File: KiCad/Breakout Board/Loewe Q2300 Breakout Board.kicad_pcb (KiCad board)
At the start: 2 copper layers, 61 x 12.7 mm, 2 parts, among them J1 VGA DSUB-15, J2 JST_XH_1x10_P2.54mm_Horizontal

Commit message: Add version to PCB silkscreen.
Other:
- board text added: "Loewe Q2300 Breakout Board V.1.0"
- board text removed: "Loewe Q2300 Breakout Board"
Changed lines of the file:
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@@
 		(layer "Edge.Cuts")
 	)
-	(gr_text "Loewe Q2300\nBreakout Board"
+	(gr_text "Loewe Q2300\nBreakout Board V.1.0"
 		(at 160.35 95.95 0)
 		(layer "B.SilkS")

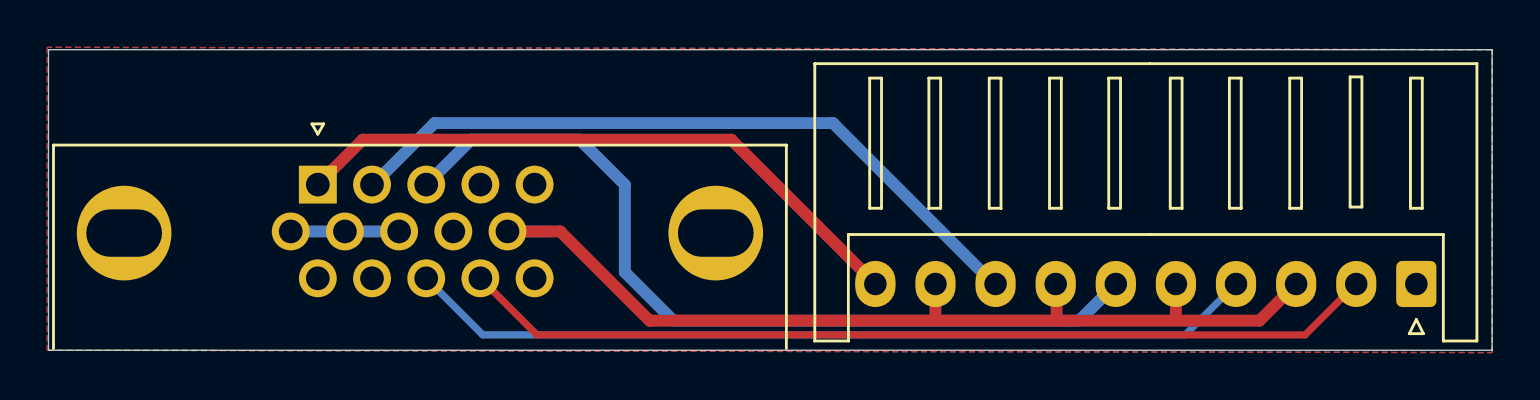
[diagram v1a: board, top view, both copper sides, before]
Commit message: Replace incorrect Connector_Dsub:DSUB-15-HD_Male with Connector_Dsub:DSUB-15-HD_Female.
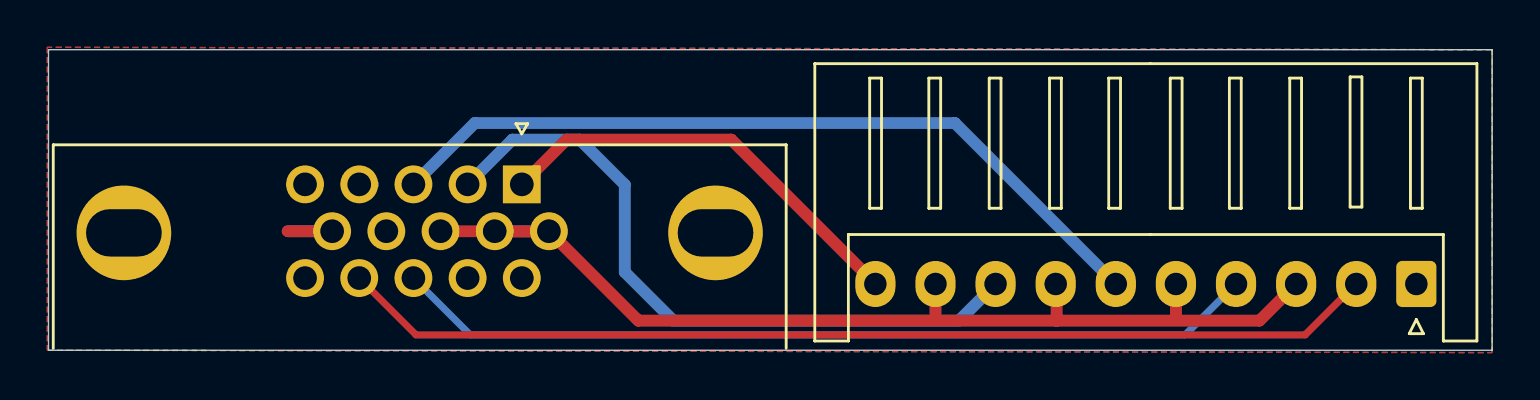
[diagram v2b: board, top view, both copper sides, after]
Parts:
- J1: footprint Connector_Dsub:DSUB-15-HD_Male_Horizontal_P2.29x1.98mm_EdgePinOffset3.03mm_Housed_MountingHolesOffset4.94mm -> Connector_Dsub:DSUB-15-HD_Female_Horizontal_P2.29x1.98mm_EdgePinOffset3.03mm_Housed_MountingHolesOffset4.94mm
- moved J1 8.62 mm to (121.8, 96.4)
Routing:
- net /RED_B: track 26.9 -> 18.3 mm
- net /VSYNC_B: track 38.9 -> 44.0 mm
- net /BLUE_B: track 35.9 -> 33.6 mm
- net /GND_B: track 46.4 -> 48.4 mm
- net /GREEN_B: track 30.2 -> 29.1 mm
- net /HSYNC_B: track 36.1 -> 36.6 mm
